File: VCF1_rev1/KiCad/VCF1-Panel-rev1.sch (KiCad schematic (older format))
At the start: 22 parts, among them Q1 Q_NPN_BCE, Q2 Q_NPN_BCE, SW1 SW_SPDT_MSM, SW2 SW_SPDT_MSM

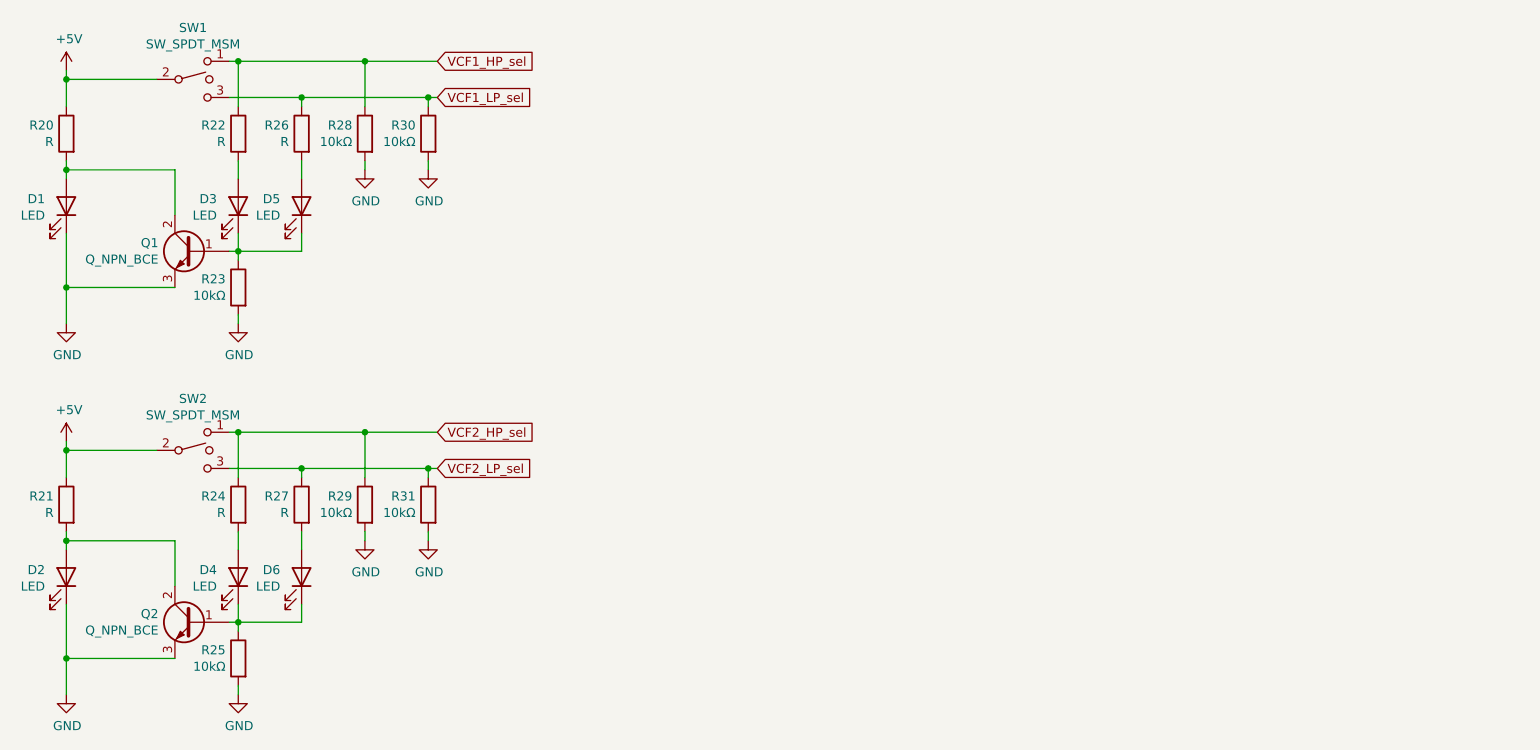
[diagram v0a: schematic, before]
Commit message: Added some initial resonance control and some other stuff.
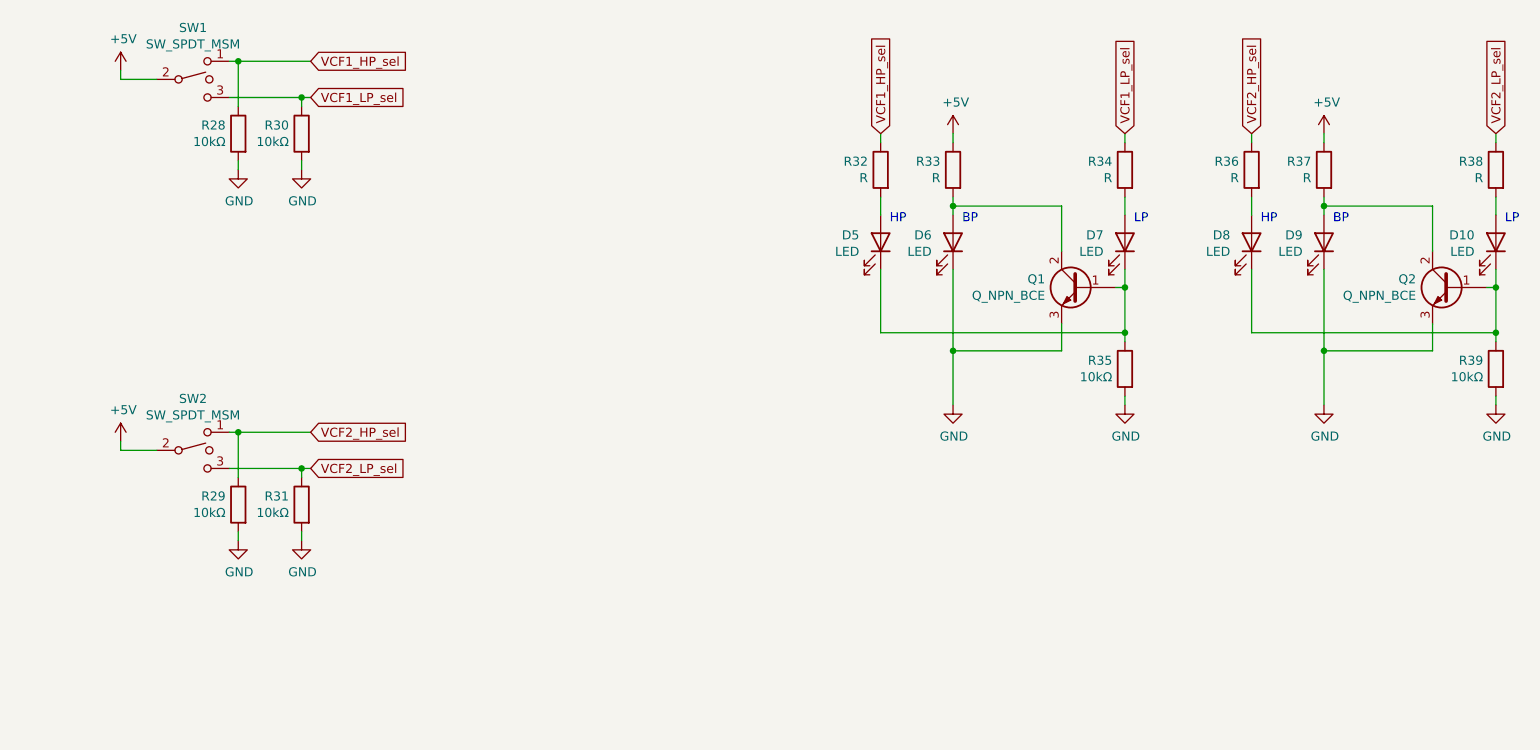
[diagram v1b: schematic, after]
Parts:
- removed D2, D4, D6: LED, symbol Device:LED
- removed R21, R24, R27: R, symbol Device:R
- removed R25: 10kΩ, symbol Device:R
- added D10, D8, D9: LED, symbol Device:LED
- added R36, R37, R38: R, symbol Device:R
- added R39: 10kΩ, symbol Device:R
- renumbered D3 to D5, D1 to D6, D5 to D7, R22 to R32, R20 to R33, R26 to R34, R23 to R35
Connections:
- net +5V: now also R37.1
- net GND: now also D9.1 (K), R39.2
- net VCF2_HP_sel: now also R36.1
- net VCF2_LP_sel: now also R38.1
- net at Q2.1 (B): now also D10.1 (K), D8.1 (K), R39.1
- net at Q2.2 (C): now also D9.2 (A), R37.2
- new net: D10.2 (A), R38.2
- new net: D8.2 (A), R36.2
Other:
- note added: "BP"
- note added: "HP"
- note added: "LP"
- moved on the sheet: D5, D6, D7, Q1, R28, R29, R30, R31, R32, R33, R34, R35
